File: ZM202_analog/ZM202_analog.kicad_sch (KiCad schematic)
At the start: 3 parts, among them U1 2N4416, U2 TL431, U3 LM324

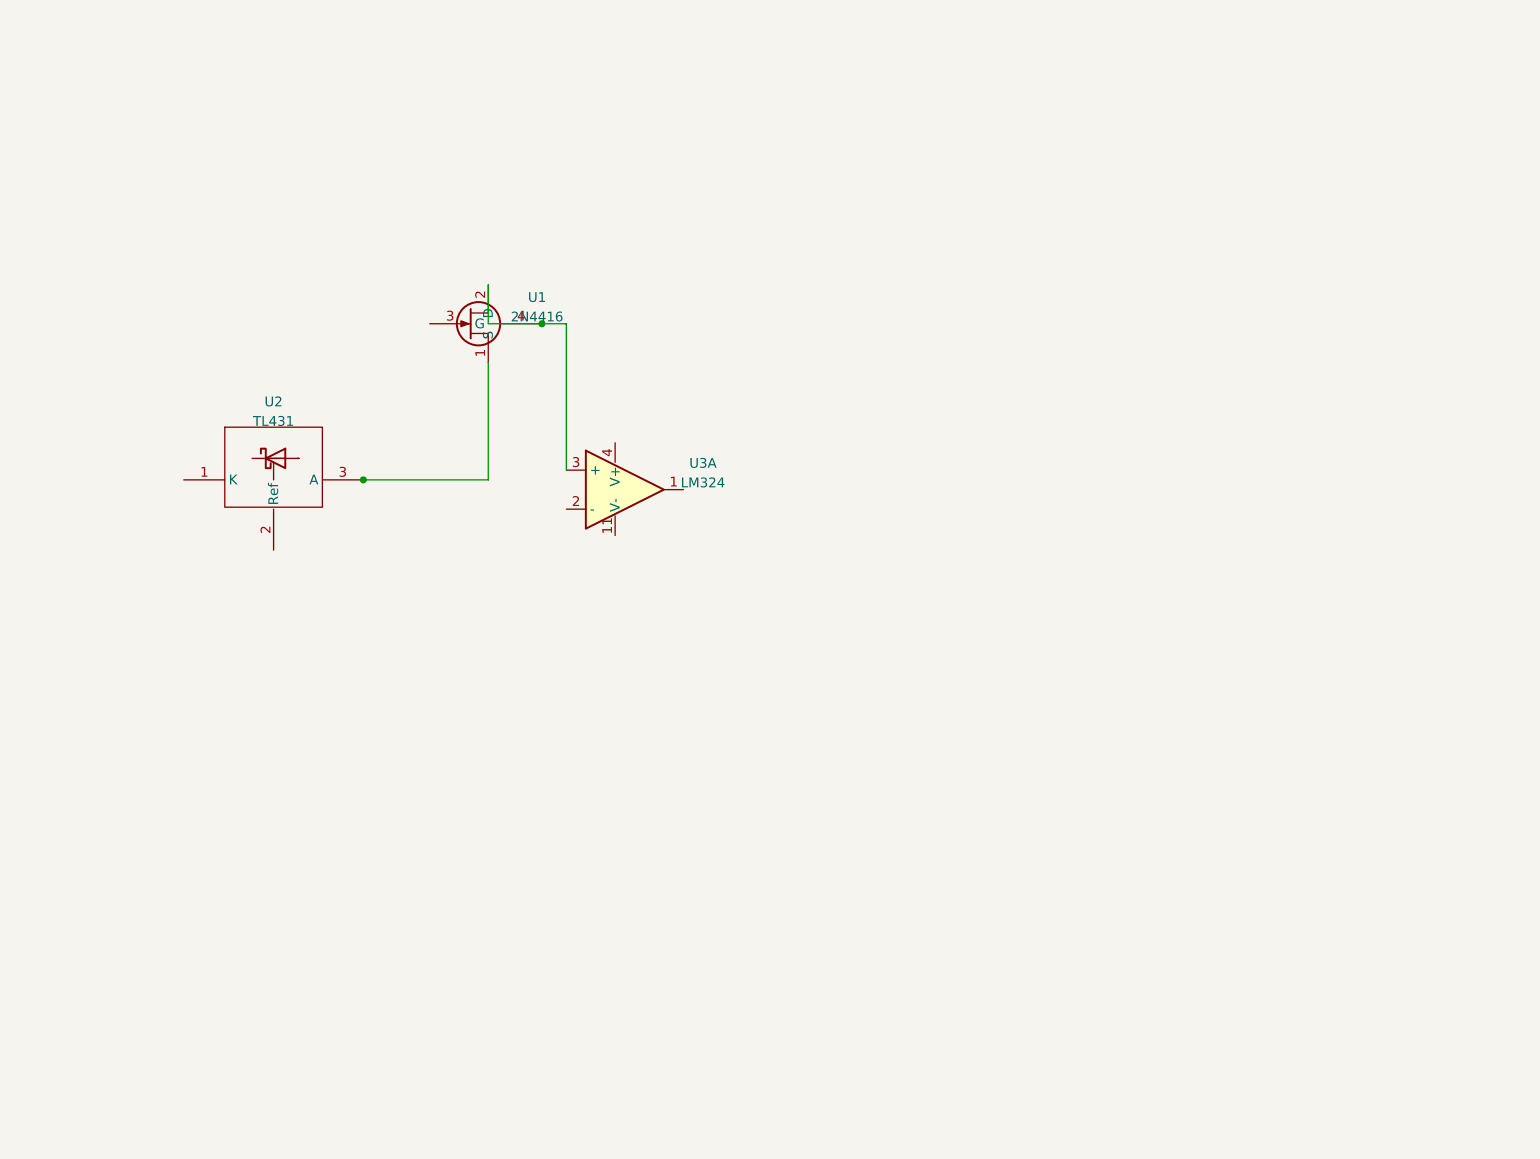
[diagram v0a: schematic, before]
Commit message: put parts into oscillator sheet
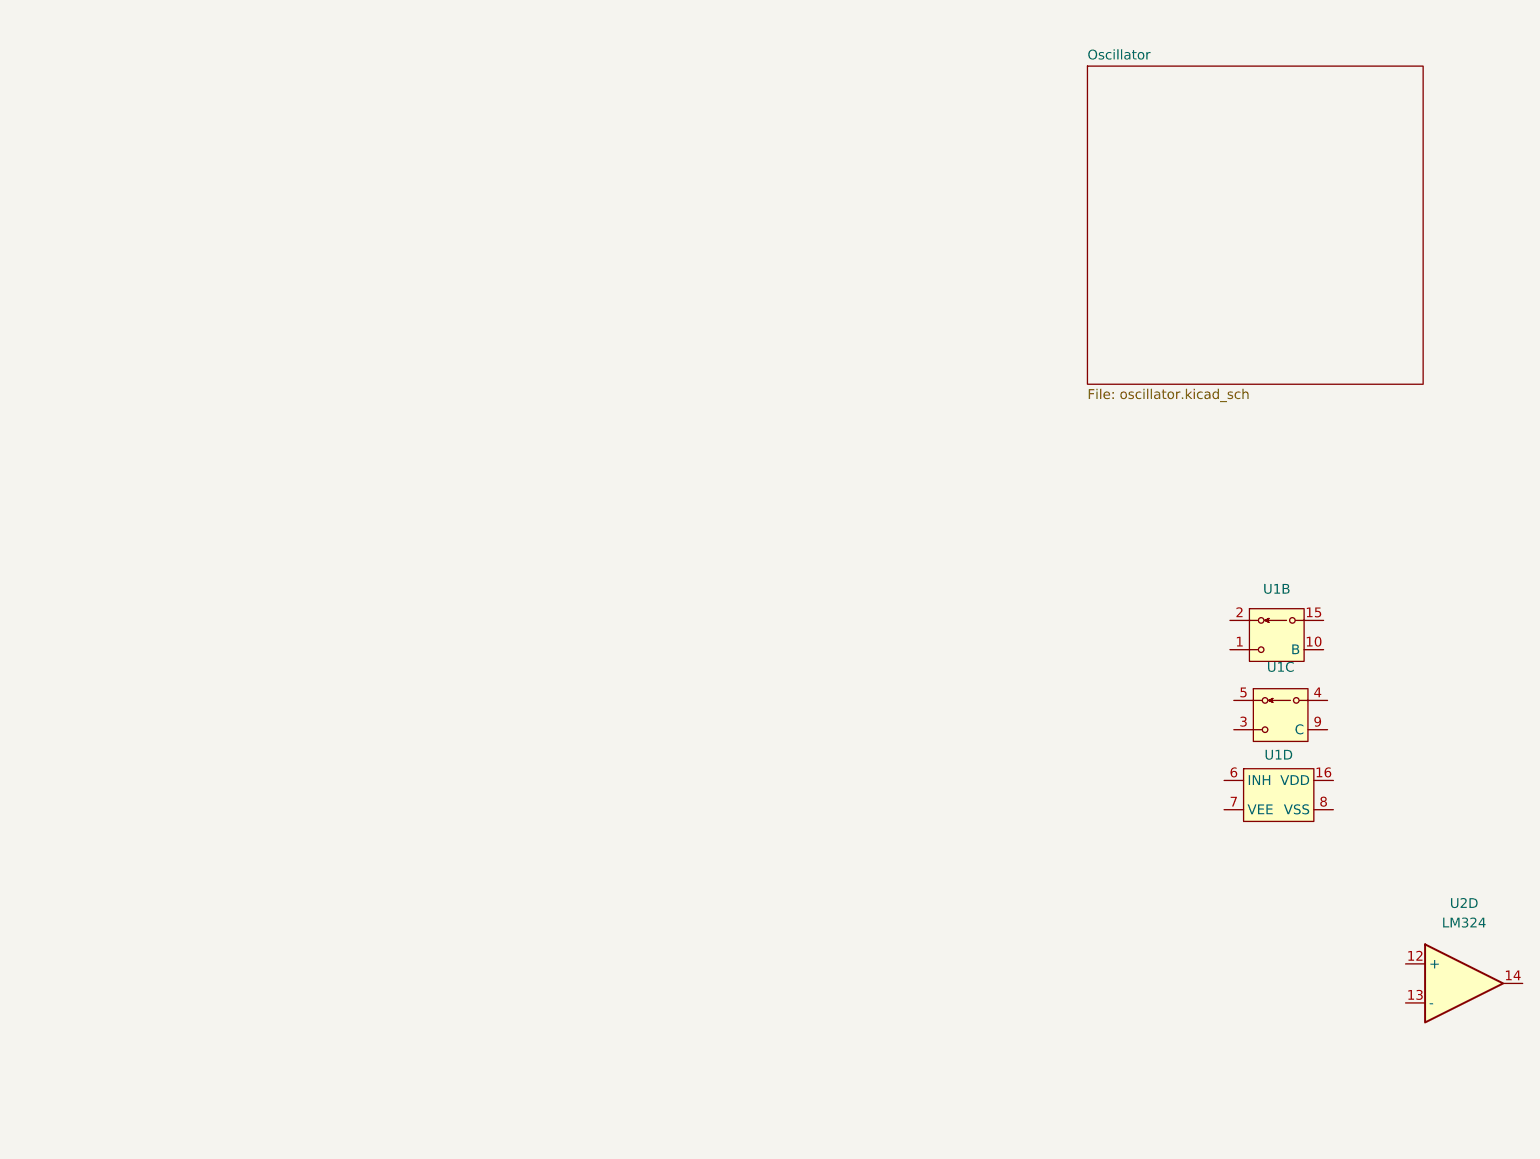
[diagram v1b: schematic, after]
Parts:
- removed U1: 2N4416, Package_TO_SOT_THT:TO-72-4, symbol Jojo_Kicad_Lib:2N4416
- removed U2: TL431, Package_TO_SOT_SMD:SOT-23, symbol Jojo_Kicad_Lib:TL431
- removed U3: LM324, Package_SO:SO-14_3.9x8.65mm_P1.27mm, symbol Jojo_Kicad_Lib:LM324ADR
- added U1: ~, Package_SO:SOIC-16W_5.3x10.2mm_P1.27mm, symbol Jojos_Lib:CD4053
- added U2: LM324, Package_SO:SO-14_3.9x8.65mm_P1.27mm, symbol Jojos_Lib:LM324ADR
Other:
- added sheet Oscillator (oscillator.kicad_sch)
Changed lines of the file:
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@@
 (kicad_sch (version 20230121) (generator eeschema)
   (paper "A4")
-  (junction (at 81.534 86.36) (diameter 0) (color 0 0 0 0)
-  )
-  (junction (at 104.775 66.04) (diameter 0) (color 0 0 0 0)
-  )
-  (wire (pts (xy 81.534 86.36) (xy 97.79 86.36))
-    (stroke (width 0) (type default))
-  )
-  (wire (pts (xy 97.79 66.04) (xy 104.775 66.04))
-    (stroke (width 0) (type default))
-  )
-  (wire (pts (xy 81.28 86.36) (xy 81.534 86.36))
-    (stroke (width 0) (type default))
-  )
-  (wire (pts (xy 97.79 86.36) (xy 97.79 71.12))
-    (stroke (width 0) (type default))
-  )
-  (wire (pts (xy 104.775 66.04) (xy 107.95 66.04))
-    (stroke (width 0) (type default))
-  )
-  (wire (pts (xy 107.95 66.04) (xy 107.95 85.09))
-    (stroke (width 0) (type default))
-  )
-  (wire (pts (xy 97.79 66.04) (xy 97.79 60.96))
-    (stroke (width 0) (type default))
-  )
-  (symbol (lib_id "Jojo_Kicad_Lib:2N4416") (at 101.6 66.04 0) (unit 1)
+  (symbol (lib_id "Jojos_Lib:CD4053") (at 199.898 117.094 0) (unit 3)
     (in_bom yes) (on_board yes) (dnp no) (fields_autoplaced)
-    (property "Reference" "U1" (at 104.14 62.6111 0)
+    (property "Reference" "U1" (at 200.914 110.744 0)
       (effects (font (size 1.27 1.27)))
     )
-    (property "Value" "2N4416" (at 104.14 65.1511 0)
+    (property "Value" "~" (at 198.374 117.348 0)
       (effects (font (size 1.27 1.27)))
     )
-    (property "Footprint" "Package_TO_SOT_THT:TO-72-4" (at 101.6 66.04 0)
+    (property "Footprint" "Package_SO:SOIC-16W_5.3x10.2mm_P1.27mm" (at 198.374 117.348 0)
       (effects (font (size 1.27 1.27)) hide)
     )
-    (property "Datasheet" "" (at 101.6 66.04 0)
+    (property "Datasheet" "" (at 198.374 117.348 0)
       (effects (font (size 1.27 1.27)) hide)
     )
-    (property "Mouser Part Number" "610-2N4416A " (at 101.6 66.04 0)
+    (property "Mouser Part Number" "595-CD4053BM96G3" (at 199.898 117.094 0)
       (effects (font (size 1.27 1.27)) hide)
     )
-    (property "Place" "yes" (at 101.6 66.04 0)
-      (effects (font (size 1.27 1.27)) hide)
-    )
+    (pin "11")
+    (pin "12")
+    (pin "13")
+    (pin "14")
     (pin "1")
+    (pin "10")
+    (pin "15")
     (pin "2")
     (pin "3")
     (pin "4")
+    (pin "5")
+    (pin "9")
+    (pin "16")
+    (pin "6")
+    (pin "7")
+    (pin "8")
     (instances
       (project "ZM202_analog"
         (path "/99a04650-e6a5-4da0-b985-3216476cb3cd"
-          (reference "U1") (unit 1)
+          (reference "U1") (unit 3)
         )
       )
     )
   )
-  (symbol (lib_id "Jojo_Kicad_Lib:LM324ADR ") (at 113.03 87.63 0) (unit 1)
+  (symbol (lib_id "Jojos_Lib:LM324ADR ") (at 222.25 151.892 0) (unit 4)
     (in_bom yes) (on_board yes) (dnp no) (fields_autoplaced)
-    (property "Reference" "U3" (at 125.73 84.2011 0)
+    (property "Reference" "U2" (at 224.79 141.478 0)
       (effects (font (size 1.27 1.27)))
     )
-    (property "Value" "LM324" (at 125.73 86.7411 0)
+    (property "Value" "LM324" (at 224.79 144.018 0)
       (effects (font (size 1.27 1.27)))
     )
-    (property "Footprint" "Package_SO:SO-14_3.9x8.65mm_P1.27mm" (at 113.03 87.63 0)
+    (property "Footprint" "Package_SO:SO-14_3.9x8.65mm_P1.27mm" (at 222.25 151.892 0)
       (effects (font (size 1.27 1.27)) hide)
     )
-    (property "Datasheet" "" (at 113.03 87.63 0)
+    (property "Datasheet" "" (at 222.25 151.892 0)
       (effects (font (size 1.27 1.27)) hide)
     )
-    (property "Mouser Part Number" "595-LM324ADR " (at 113.03 87.63 0)
+    (property "Mouser Part Number" "595-LM324ADR " (at 222.25 151.892 0)
       (effects (font (size 1.27 1.27)) hide)
     )
-    (property "Place" "yes" (at 113.03 87.63 0)
+    (property "Place" "yes" (at 222.25 151.892 0)
       (effects (font (size 1.27 1.27)) hide)
     )
@@
       (project "ZM202_analog"
         (path "/99a04650-e6a5-4da0-b985-3216476cb3cd"
-          (reference "U3") (unit 1)
+          (reference "U2") (unit 4)
         )
       )
     )
   )
-  (symbol (lib_id "Jojo_Kicad_Lib:TL431") (at 69.85 86.36 0) (unit 1)
+  (symbol (lib_id "Jojos_Lib:CD4053") (at 199.898 106.426 0) (unit 2)
     (in_bom yes) (on_board yes) (dnp no) (fields_autoplaced)
-    (property "Reference" "U2" (at 69.85 76.2 0)
+    (property "Reference" "U1" (at 200.406 100.584 0)
       (effects (font (size 1.27 1.27)))
     )
-    (property "Value" "TL431" (at 69.85 78.74 0)
+    (property "Value" "~" (at 198.374 106.68 0)
       (effects (font (size 1.27 1.27)))
     )
-    (property "Footprint" "Package_TO_SOT_SMD:SOT-23" (at 69.85 86.36 0)
+    (property "Footprint" "Package_SO:SOIC-16W_5.3x10.2mm_P1.27mm" (at 198.374 106.68 0)
       (effects (font (size 1.27 1.27)) hide)
     )
-    (property "Datasheet" "" (at 69.85 86.36 0)
+    (property "Datasheet" "" (at 198.374 106.68 0)
       (effects (font (size 1.27 1.27)) hide)
     )
-    (property "Mouser Part Number" "771-TL431AQDBZR215" (at 69.85 86.36 0)
+    (property "Mouser Part Number" "595-CD4053BM96G3" (at 199.898 106.426 0)
       (effects (font (size 1.27 1.27)) hide)
     )
-    (property "Place" "yes" (at 69.85 86.36 0)
-      (effects (font (size 1.27 1.27)) hide)
-    )
+    (pin "11")
+    (pin "12")
+    (pin "13")
+    (pin "14")
     (pin "1")
+    (pin "10")
+    (pin "15")
     (pin "2")
     (pin "3")
+    (pin "4")
+    (pin "5")
+    (pin "9")
+    (pin "16")
+    (pin "6")
+    (pin "7")
+    (pin "8")
     (instances
       (project "ZM202_analog"
         (path "/99a04650-e6a5-4da0-b985-3216476cb3cd"
-          (reference "U2") (unit 1)
+          (reference "U1") (unit 2)
         )
       )
     )
+  )
+  (symbol (lib_id "Jojos_Lib:CD4053") (at 200.66 127 0) (unit 4)
+    (in_bom yes) (on_board yes) (dnp no) (fields_autoplaced)
+    (property "Reference" "U1" (at 200.66 122.174 0)
+      (effects (font (size 1.27 1.27)))
+    )
+    (property "Value" "~" (at 199.136 127.254 0)
+      (effects (font (size 1.27 1.27)))
+    )
+    (property "Footprint" "Package_SO:SOIC-16W_5.3x10.2mm_P1.27mm" (at 199.136 127.254 0)
+      (effects (font (size 1.27 1.27)) hide)
+    )
+    (property "Datasheet" "" (at 199.136 127.254 0)
+      (effects (font (size 1.27 1.27)) hide)
+    )
+    (property "Mouser Part Number" "595-CD4053BM96G3" (at 200.66 127 0)
+      (effects (font (size 1.27 1.27)) hide)
+    )
+    (pin "11")
+    (pin "12")
+    (pin "13")
+    (pin "14")
+    (pin "1")
+    (pin "10")
+    (pin "15")
+    (pin "2")
+    (pin "3")
+    (pin "4")
+    (pin "5")
+    (pin "9")
+    (pin "16")
+    (pin "6")
+    (pin "7")
+    (pin "8")
+    (instances
+      (project "ZM202_analog"
+        (path "/99a04650-e6a5-4da0-b985-3216476cb3cd"
+          (reference "U1") (unit 4)
+        )
+      )
+    )
+  )
+  (sheet (at 175.768 32.512) (size 43.688 41.402) (fields_autoplaced)
+    (stroke (width 0.1524) (type solid))
+    (fill (color 0 0 0 0.0000))
+    (property "Sheetname" "Oscillator" (at 175.768 31.8004 0)
+      (effects (font (size 1.27 1.27)) (justify left bottom))
+    )
+    (property "Sheetfile" "oscillator.kicad_sch" (at 175.768 74.4986 0)
+      (effects (font (size 1.27 1.27)) (justify left top))
+    )
+    (instances
+      (project "ZM202_analog"
+        (path "/99a04650-e6a5-4da0-b985-3216476cb3cd" (page "2"))
+      )
+    )
